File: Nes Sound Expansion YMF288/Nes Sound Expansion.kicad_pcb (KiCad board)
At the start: 2 copper layers, 41.9 x 87.6 mm, 45 parts, among them J1 NES-SNES Port1, J2 NES-SNES Port2, J3 EXP 1-24, J4 EXP 25-48, J5 EN Switch, J6 AudioJack2_Ground_Switch, J7 EN LED, U1 74HC139D, U10 74HC257D, U2 74HC132D, U6 74HC174D, U7 74HC174D, U8 74HC257D, U9 74HC257D, X1 CXO_DIP8

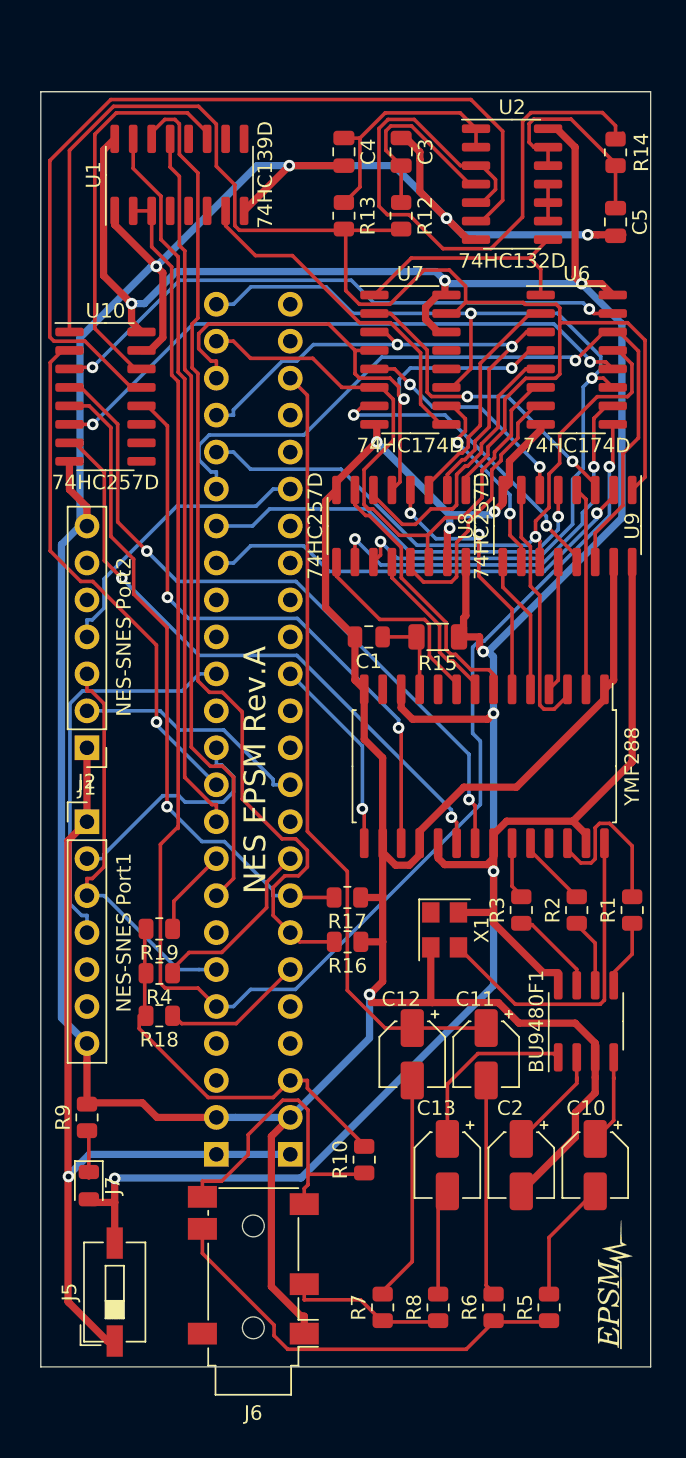
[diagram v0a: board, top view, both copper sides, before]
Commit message: Added amplification for both famicom and nes model
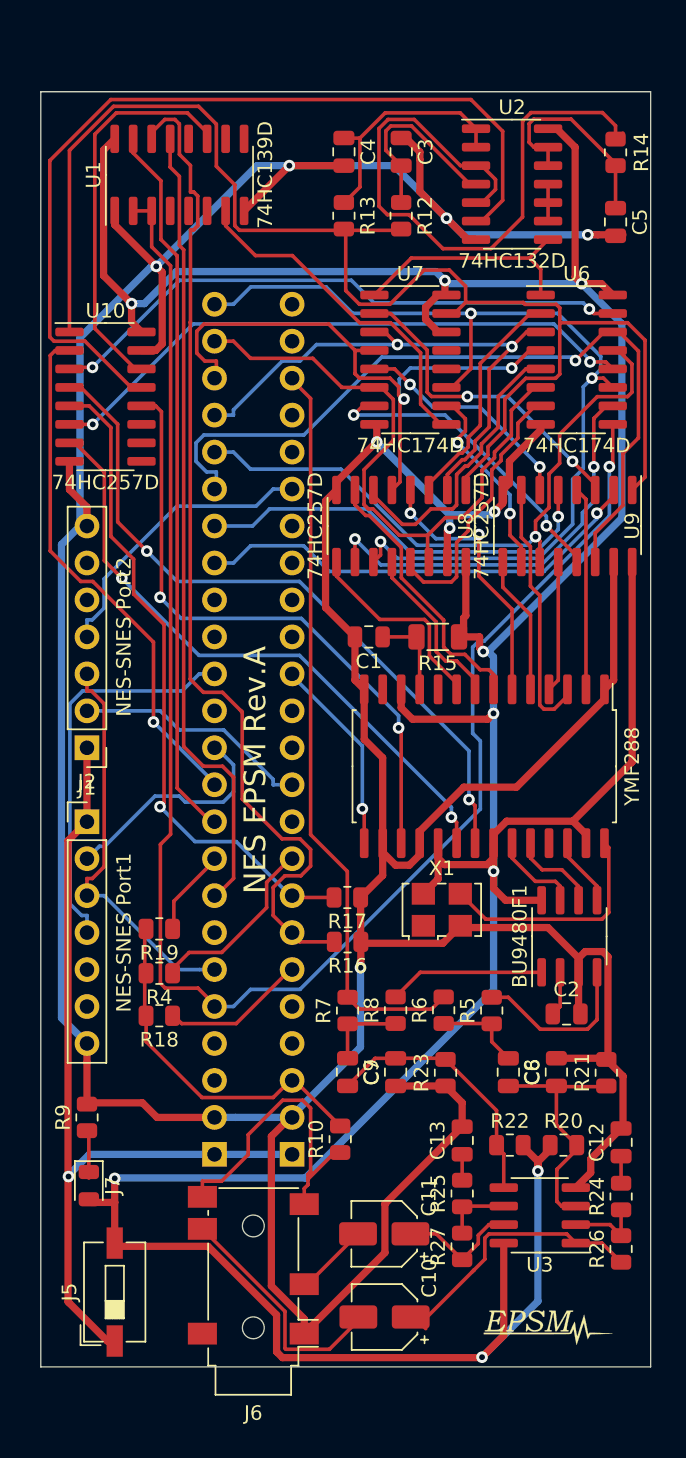
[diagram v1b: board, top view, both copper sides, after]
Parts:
- removed R1, R2, R3: 1k, Resistor_SMD:R_0805_2012Metric
- added C6: 10uF, Capacitor_SMD:C_0805_2012Metric, F.Cu at (128.0, 103.6)
- added C7: 10uF, Capacitor_SMD:C_0805_2012Metric, F.Cu at (117.0, 103.6)
- added C8: 68pF, Capacitor_SMD:C_0805_2012Metric, F.Cu at (131.3, 103.6)
- added C9: 68pF, Capacitor_SMD:C_0805_2012Metric, F.Cu at (120.3, 103.6)
- added R20: 47k, Resistor_SMD:R_0805_2012Metric, F.Cu at (131.8, 108.6)
- added R21: 47k, Resistor_SMD:R_0805_2012Metric, F.Cu at (134.7, 103.6)
- added R22: 47k, Resistor_SMD:R_0805_2012Metric, F.Cu at (128.1, 108.6)
- added R23: 47k, Resistor_SMD:R_0805_2012Metric, F.Cu at (123.7, 103.6)
- added R24: 3k, Resistor_SMD:R_0805_2012Metric, F.Cu at (135.8, 112.1)
- added R25: 3k, Resistor_SMD:R_0805_2012Metric, F.Cu at (124.8, 111.9)
- added R26: 47k, Resistor_SMD:R_0805_2012Metric, F.Cu at (135.8, 115.7)
- added R27: 47k, Resistor_SMD:R_0805_2012Metric, F.Cu at (124.8, 115.5)
- added U3: LM358, Package_SO:SOIC-8_3.9x4.9mm_P1.27mm, F.Cu at (130.2, 113.4)
- C12, C13, C2: footprint Capacitor_SMD:CP_Elec_4x5.3 -> Capacitor_SMD:C_0805_2012Metric
- R10: value 1k -> 10k
- X1: footprint Oscillator:Oscillator_SMD_SeikoEpson_SG8002CE-4Pin_3.2x2.5mm -> Oscillator:Oscillator_SMD_SeikoEpson_SG8002LB-4Pin_5.0x3.2mm
- moved R5 20.8 mm to (126.9, 99.3)
- moved R6 20.7 mm to (123.6, 99.3)
- moved R8 20.6 mm to (120.3, 99.3)
- moved R7 20.5 mm to (117.0, 99.3)
- moved C10 17.8 mm to (119.5, 120.4), turned to 180 degrees
- moved C12 15.6 mm to (135.8, 108.4), turned to 90 degrees
- moved C11 14.2 mm to (119.5, 114.7), turned to 180 degrees
- moved C2 10.8 mm to (132.0, 99.6), turned to 0 degrees
- moved BU9480F1 5.96 mm to (132.2, 94.2)
- moved G*** 5.29 mm to (130.9, 121.0), turned to 0 degrees
- moved R10 2.17 mm to (116.5, 108.2)
- moved C13 1.98 mm to (124.8, 108.3), turned to 90 degrees
- moved X1 1.40 mm to (123.4, 92.4), turned to 0 degrees
- moved J4 0.13 mm to (107.8, 109.2)
- moved J3 0.13 mm to (113.2, 109.2)
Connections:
- C10 pad 1: Net-(BU9480F1-Pad4) -> Net-(C10-Pad1)
- C11 pad 1: Aud -> Net-(C11-Pad1)
- C12 pad 1: Aud -> Net-(C12-Pad1)
- C12 pad 2: Net-(C12-Pad2) -> GND
- C13 pad 1: Net-(BU9480F1-Pad1) -> Net-(C13-Pad1)
- C13 pad 2: Net-(C13-Pad2) -> GND
- J6 pad S: Net-(J6-PadS) -> Net-(C11-Pad2)
- J6 pad T: Net-(J6-PadT) -> Net-(C10-Pad2)
- R5 pad 1: Net-(J6-PadT) -> Net-(C6-Pad1)
- R5 pad 2: Net-(C10-Pad2) -> Net-(BU9480F1-Pad4)
- R6 pad 1: Net-(J6-PadT) -> Net-(C6-Pad1)
- R6 pad 2: Net-(C11-Pad2) -> Aud
- R7 pad 1: Net-(J6-PadS) -> Net-(C7-Pad1)
- R7 pad 2: Net-(C12-Pad2) -> Aud
- R8 pad 1: Net-(J6-PadS) -> Net-(C7-Pad1)
- R8 pad 2: Net-(C13-Pad2) -> Net-(BU9480F1-Pad1)
- YMF288 pad 23: Net-(R3-Pad2) -> Net-(BU9480F1-Pad7)
- YMF288 pad 24: Net-(R2-Pad2) -> Net-(BU9480F1-Pad6)
- YMF288 pad 26: Net-(R1-Pad2) -> Net-(BU9480F1-Pad5)
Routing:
- net +5V: track 221.5 -> 275.2 mm, vias 7 -> 9
- net GND: track 307.1 -> 340.1 mm
- net Net-(J6-PadT): track 29.4 -> 0.00 mm
- net Net-(C10-Pad1): track 0.00 -> 19.8 mm
- net Net-(C7-Pad2): track 0.00 -> 17.4 mm
- net Net-(C6-Pad2): track 0.00 -> 17.0 mm
- net Net-(C12-Pad2): track 15.4 -> 0.00 mm
- net Net-(R1-Pad2): track 11.7 -> 0.00 mm
- net Net-(J6-PadS): track 10.9 -> 0.00 mm
- net Net-(C11-Pad2): track 14.8 -> 5.13 mm
- net Net-(C10-Pad2): track 8.29 -> 16.8 mm
- net Net-(C11-Pad1): track 0.00 -> 8.48 mm
- net Net-(C13-Pad2): track 7.24 -> 0.00 mm
- net Net-(X1-Pad3): track 22.6 -> 16.0 mm
- net Net-(C6-Pad1): track 0.00 -> 6.16 mm
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
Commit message: Removed power switch and updated resistor values
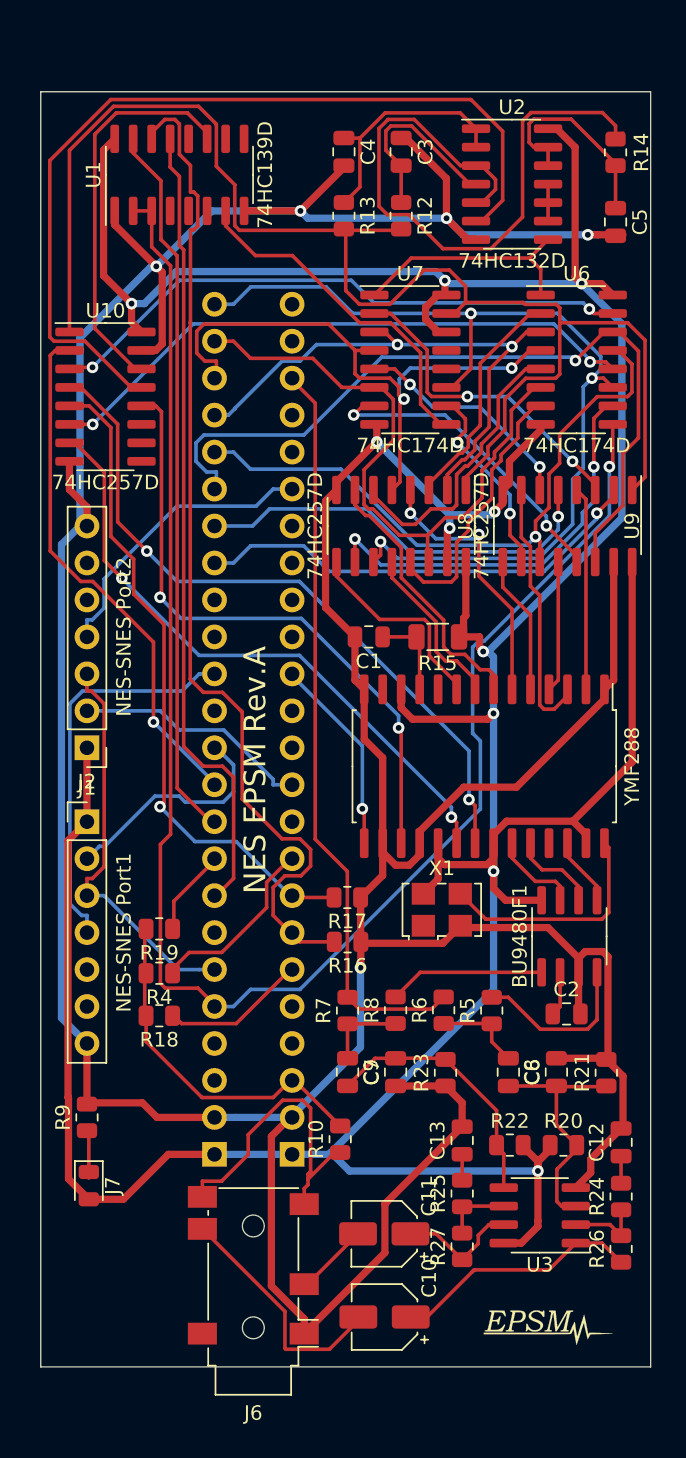
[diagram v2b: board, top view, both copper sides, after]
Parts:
- removed J5: EN Switch, Button_Switch_SMD:SW_DIP_SPSTx01_Slide_6.7x4.1mm_W6.73mm_P2.54mm_LowProfile_JPin
- R10: value 10k -> 47k
- R13: value 1k -> 3k
- R21, R23: value 47k -> 33k
- R24, R25: value 3k -> 8.2k
- R26, R27: value 47k -> 22k
- R5, R8: value 560 -> 680
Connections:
- J1 pad 1: Net-(J1-Pad1) -> +5V
- J2 pad 1: Net-(J1-Pad1) -> +5V
- J3 pad 1: Net-(J1-Pad1) -> +5V
- J4 pad 1: Net-(J1-Pad1) -> +5V
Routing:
- net Net-(J1-Pad1): track 58.8 -> 0.00 mm, vias 1 -> 0
- net +5V: track 275.2 -> 271.9 mm, vias 9 -> 7
- net GND: track 340.1 -> 337.5 mm
- net Net-(C10-Pad1): track 19.8 -> 17.3 mm

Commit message: Updated Rev.A to Rev.A1
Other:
- board text added: "NES EPSM Rev.A1"

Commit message: Update Rev.B
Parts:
- removed J2: NES-SNES Port2, Connector_PinHeader_2.54mm:PinHeader_1x07_P2.54mm_Vertical
- C3, C4, C5, C8, C9: footprint Capacitor_SMD:C_0805_2012Metric -> Capacitor_SMD:C_0603_1608Metric
- J1: value NES-SNES Port1 -> DA15_Plug; footprint Connector_PinHeader_2.54mm:PinHeader_1x07_P2.54mm_Vertical -> Connector_IDC:IDC-Header_2x08_P2.54mm_Vertical
- J6: footprint audioconn:Jack_3.5mm_PJ311_Horizontal -> audioconn:Jack_3.5mm_PJ311_Horizontal_other_pinout
- R10: value 47k -> 0ohm; footprint Resistor_SMD:R_0805_2012Metric -> Resistor_SMD:R_0603_1608Metric
- R12, R13, R14, R16, R17, R18, R19, R20, R21, R22, R23, R26, R27, R4, R5, R6, R7, R8, R9: footprint Resistor_SMD:R_0805_2012Metric -> Resistor_SMD:R_0603_1608Metric
- R15: footprint Resistor_SMD:R_1206_3216Metric -> Resistor_SMD:R_0603_1608Metric
- R24, R25: value 8.2k -> 6.8k; footprint Resistor_SMD:R_0805_2012Metric -> Resistor_SMD:R_0603_1608Metric
- moved G*** 79.3 mm to (100.6, 47.8), turned to -90 degrees
- moved R27 77.0 mm to (126.9, 38.6), turned to 0 degrees
- moved U1 75.2 mm to (101.3, 117.0), turned to 0 degrees
- moved C10 74.6 mm to (119.9, 45.8)
- moved C11 74.6 mm to (119.9, 40.1)
- moved J6 73.8 mm to (110.5, 43.1), turned to 0 degrees
- moved R25 73.5 mm to (130.6, 38.6), turned to 0 degrees
- moved C13 70.1 mm to (134.4, 38.9), turned to 0 degrees
- moved U3 69.5 mm to (128.8, 43.9), turned to 90 degrees
- moved R26 67.1 mm to (126.7, 49.3), turned to 0 degrees
- moved R22 66.7 mm to (133.9, 42.1), turned to -90 degrees
- moved R24 63.1 mm to (130.3, 49.3), turned to 0 degrees
- moved R20 62.8 mm to (133.9, 45.8), turned to -90 degrees
- moved C12 59.1 mm to (134.1, 49.3), turned to 0 degrees
- moved C7 52.8 mm to (134.1, 53.6), turned to 90 degrees
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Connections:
- J1 pad 1: +5V -> Joy1_D2
- J1 pad 2: Joy1_OE -> Joy2_D0
- J1 pad 3: OUT0 -> +5V
- J1 pad 4: Joy1_D0 -> Joy2_D1
- J1 pad 5: (no net) -> Joy1_OE
- J1 pad 6: (no net) -> Joy2_D2
- J1 pad 7: GND -> Joy1_D1
- J3 pad 10: (no net) -> unconnected-(J3-Pin_10-Pad10)
- J3 pad 12: (no net) -> Joy1_D1
- J3 pad 13: (no net) -> Joy1_D3
- J3 pad 15: (no net) -> Joy2_D2
- J3 pad 16: (no net) -> Joy2_D3
- J3 pad 17: (no net) -> unconnected-(J3-Pin_17-Pad17)
- J3 pad 18: (no net) -> Joy2_D4
- J3 pad 20: (no net) -> Joy2_D1
- J3 pad 21: (no net) -> unconnected-(J3-Pin_21-Pad21)
- J3 pad 23: (no net) -> unconnected-(J3-Pin_23-Pad23)
- J3 pad 24: (no net) -> unconnected-(J3-Pin_24-Pad24)
- J3 pad 4: (no net) -> NMI
- J3 pad 5: (no net) -> unconnected-(J3-Pin_5-Pad5)
- J4 pad 13: (no net) -> Joy1_D4
- J4 pad 15: (no net) -> unconnected-(J4-Pin_15-Pad15)
- J4 pad 16: (no net) -> Joy1_D2
- J4 pad 3: (no net) -> unconnected-(J4-Pin_3-Pad3)
- J4 pad 4: (no net) -> OUT2
- J4 pad 7: (no net) -> unconnected-(J4-Pin_7-Pad7)
- U1 pad 10: (no net) -> unconnected-(U1B-O2-Pad10)
- U1 pad 12: (no net) -> unconnected-(U1B-O0-Pad12)
- U1 pad 4: (no net) -> unconnected-(U1A-O0-Pad4)
- U1 pad 5: (no net) -> unconnected-(U1A-O1-Pad5)
- U1 pad 6: (no net) -> unconnected-(U1A-O2-Pad6)
- U1 pad 9: (no net) -> unconnected-(U1B-O3-Pad9)
- U10 pad 10: (no net) -> unconnected-(U10-I1d-Pad10)
- U10 pad 11: (no net) -> unconnected-(U10-I0d-Pad11)
- U10 pad 9: (no net) -> unconnected-(U10-Zd-Pad9)
- U7 pad 12: (no net) -> unconnected-(U7-Q4-Pad12)
- U7 pad 13: (no net) -> unconnected-(U7-D4-Pad13)
- U8 pad 10: D7_buf -> D6_buf
- U8 pad 11: D7 -> D6
- U8 pad 12: D6_Chip -> D7_Chip
- U8 pad 13: D6_buf -> D7_buf
- U8 pad 14: D6 -> D7
- U8 pad 2: D4 -> D5
- U8 pad 3: D4_buf -> D5_buf
- U8 pad 4: D4_Chip -> D5_Chip
- U8 pad 5: D5 -> D4
- U8 pad 6: D5_buf -> D4_buf
- U8 pad 7: D5_Chip -> D4_Chip
- U8 pad 9: D7_Chip -> D6_Chip
- X1 pad 1: (no net) -> unconnected-(X1-~{ST}-Pad1)
- YMF288 pad 10: (no net) -> unconnected-(YMF288-NC-Pad10)
- YMF288 pad 13: (no net) -> unconnected-(YMF288-NC-Pad13)
- YMF288 pad 25: (no net) -> unconnected-(YMF288-MCLK-Pad25)
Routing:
- net IRQ: track 13.7 -> 72.6 mm
- net Net-(BU9480F1-LRCK): track 4.77 -> 59.6 mm, vias 0 -> 2
- net CS_buf: track 60.8 -> 6.70 mm
- net Net-(BU9480F1-SDAT): track 6.09 -> 59.8 mm, vias 0 -> 2
- net Net-(BU9480F1-BCLK): track 6.10 -> 59.5 mm, vias 0 -> 2
- net OUT1: track 114.3 -> 67.6 mm
- net Net-(J6-PadSN): track 21.6 -> 66.4 mm
- net CS_: track 27.0 -> 69.0 mm, vias 0 -> 2
- net A14: track 69.9 -> 29.0 mm
- net A1_buf: track 40.8 -> 7.26 mm, vias 2 -> 0
- net OUT1_: track 23.9 -> 54.3 mm, vias 0 -> 2
- net A0_buf: track 41.6 -> 11.6 mm, vias 2 -> 0
- net Joy1_D0: track 27.3 -> 0.00 mm
- net Joy2_D4: track 0.00 -> 27.1 mm
- net GND: track 337.5 -> 311.4 mm, vias 8 -> 7
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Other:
- net class Default removed
- net class Power removed
- board text added: "NES EPSM Rev.B"
- board text removed: "NES EPSM Rev.A"
- board text removed: "NES EPSM Rev.A1"
